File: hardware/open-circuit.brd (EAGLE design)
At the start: 90.2 x 40.6 mm, 72 parts, among them IC1 PIC16F1825SO14, IC2 74HC595D, IC3 MCP4728_QUAD_DAC, IC4 LM324D, IC6 LM27675M5_CHARGEPUMP

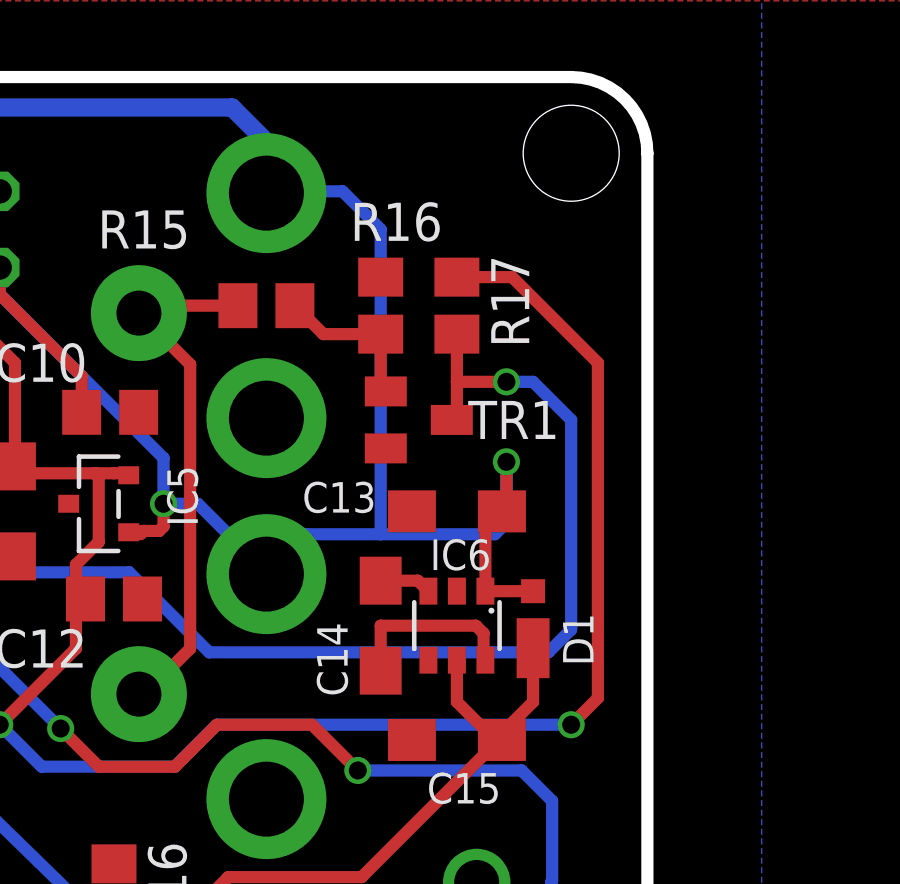
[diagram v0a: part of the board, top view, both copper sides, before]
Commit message: fix input transistor
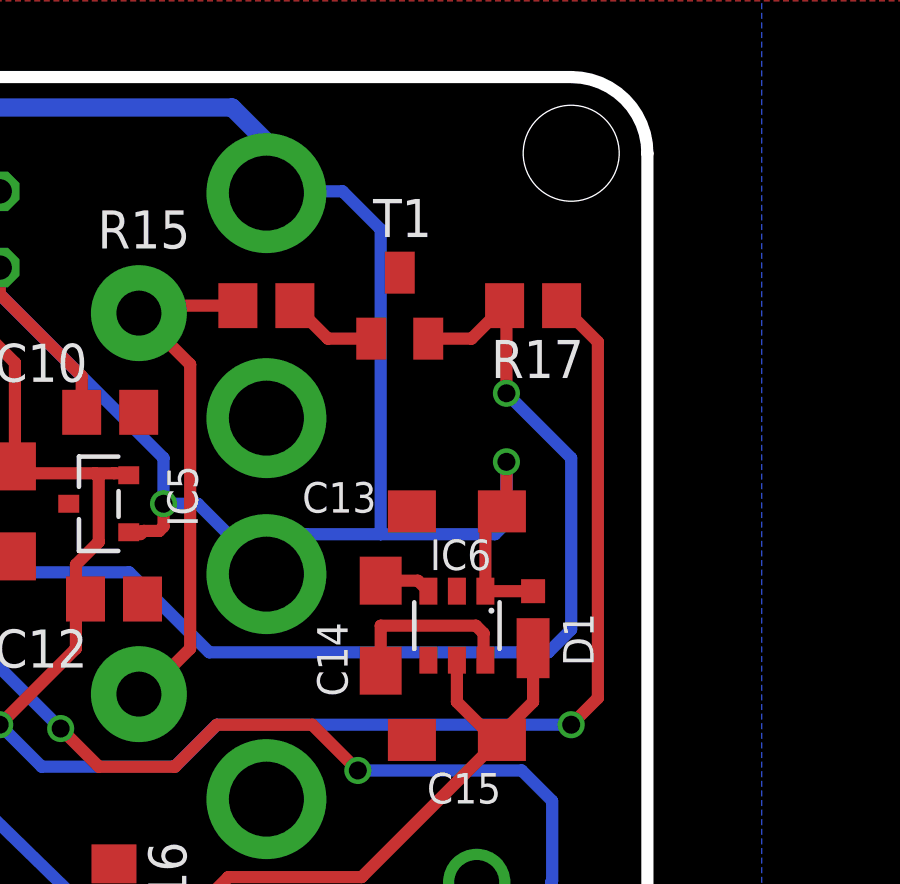
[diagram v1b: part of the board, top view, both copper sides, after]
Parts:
- removed R16: (no value), rcl:R0805
- removed TR1: (no value), transistor:SOT23-BEC
- added T1: (no value), transistor:SOT23-BEC
- moved R17 2.54 mm to (90.2, 77.5), turned to 180 degrees
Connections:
- removed net N$19: R15.1, R16.2, TR1.B
- new net N$14: R15.1, T1.B
- net GND: now also T1.C; no longer R16.1, TR1.E
- net MIDI_IN: now also T1.E; no longer TR1.C
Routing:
- net N$19: track 5.23 -> 0.00 mm
- net 3V3: track 102.9 -> 99.4 mm
- net N$14: track 0.00 -> 3.00 mm
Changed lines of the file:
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@@
 <attribute name="VALUE" x="76.2" y="72.644" size="0.4064" layer="27" rot="R90"/>
 </element>
-<element name="TR1" library="transistor" package="SOT23-BEC" value="" x="86.36" y="73.66" smashed="yes" rot="R270">
-<attribute name="NAME" x="88.011" y="73.025" size="1.27" layer="25"/>
-<attribute name="VALUE" x="83.185" y="75.565" size="1.27" layer="27" rot="R270"/>
-</element>
-<element name="R16" library="rcl" package="R0805" value="" x="85.09" y="77.47" smashed="yes" rot="R270">
-<attribute name="NAME" x="84.074" y="79.629" size="1.27" layer="25"/>
-<attribute name="VALUE" x="82.55" y="78.105" size="1.27" layer="27" rot="R270"/>
-</element>
-<element name="R17" library="rcl" package="R0805" value="" x="87.63" y="77.47" smashed="yes" rot="R270">
-<attribute name="NAME" x="90.043" y="76.073" size="1.27" layer="25" rot="R90"/>
-<attribute name="VALUE" x="85.09" y="78.105" size="1.27" layer="27" rot="R270"/>
+<element name="R17" library="rcl" package="R0805" value="" x="90.17" y="77.47" smashed="yes" rot="R180">
+<attribute name="NAME" x="88.773" y="75.057" size="1.27" layer="25"/>
+<attribute name="VALUE" x="90.805" y="80.01" size="1.27" layer="27" rot="R180"/>
 </element>
 <element name="C10" library="rcl" package="C0805" value="" x="76.073" y="73.914" smashed="yes" rot="R180">
@@
 <attribute name="NAME" x="88.646" y="56.896" size="1.27" layer="26" ratio="10" rot="MR270"/>
 <attribute name="VALUE" x="95.504" y="58.42" size="1.27" layer="28" ratio="10" rot="MR270"/>
+</element>
+<element name="T1" library="transistor" package="SOT23-BEC" value="" x="85.725" y="77.47" smashed="yes">
+<attribute name="NAME" x="84.836" y="79.756" size="1.27" layer="25"/>
+<attribute name="VALUE" x="83.82" y="74.295" size="1.27" layer="27"/>
 </element>
 </elements>
@@
 <contactref element="MIDI" pad="2"/>
 <contactref element="IC5" pad="3"/>
-<contactref element="TR1" pad="E"/>
 <contactref element="C12" pad="1"/>
 <contactref element="C13" pad="-"/>
 <contactref element="C10" pad="1"/>
-<contactref element="R16" pad="1"/>
 <contactref element="C11" pad="-"/>
 <contactref element="IC6" pad="2"/>
@@
 <via x="56.388" y="54.737" extent="1-16" drill="0.6"/>
 <contactref element="SW1" pad="2"/>
+<contactref element="T1" pad="C"/>
 </signal>
 <signal name="N$1">
@@
 </signal>
 <signal name="MIDI_IN">
-<contactref element="TR1" pad="C"/>
-<contactref element="R17" pad="2"/>
 <contactref element="IC1" pad="5"/>
-<wire x1="87.63" y1="73.83" x2="87.46" y2="73.66" width="0.4064" layer="1"/>
 <via x="60.452" y="67.691" extent="1-16" drill="0.6"/>
 <wire x1="58.36" y1="69.85" x2="59.944" y2="69.85" width="0.4064" layer="1"/>
 <wire x1="59.944" y1="69.85" x2="60.452" y2="69.342" width="0.4064" layer="1"/>
 <wire x1="60.452" y1="69.342" x2="60.452" y2="67.691" width="0.4064" layer="1"/>
-<wire x1="87.63" y1="73.83" x2="87.63" y2="74.93" width="0.4064" layer="1"/>
-<wire x1="87.63" y1="74.93" x2="89.281" y2="74.93" width="0.4064" layer="1"/>
-<via x="89.281" y="74.93" extent="1-16" drill="0.6"/>
-<wire x1="89.281" y1="74.93" x2="90.17" y2="74.93" width="0.4064" layer="16"/>
-<wire x1="90.17" y1="74.93" x2="91.44" y2="73.66" width="0.4064" layer="16"/>
-<wire x1="91.44" y1="73.66" x2="91.44" y2="66.675" width="0.4064" layer="16"/>
+<via x="89.281" y="74.549" extent="1-16" drill="0.6"/>
+<wire x1="89.281" y1="74.549" x2="91.44" y2="72.39" width="0.4064" layer="16"/>
+<wire x1="91.44" y1="72.39" x2="91.44" y2="66.675" width="0.4064" layer="16"/>
 <wire x1="91.44" y1="66.675" x2="90.678" y2="65.913" width="0.4064" layer="16"/>
 <wire x1="90.678" y1="65.913" x2="79.375" y2="65.913" width="0.4064" layer="16"/>
 <wire x1="79.375" y1="65.913" x2="76.708" y2="68.58" width="0.4064" layer="16"/>
-<wire x1="87.63" y1="76.52" x2="87.63" y2="74.93" width="0.4064" layer="1"/>
 <wire x1="60.452" y1="67.691" x2="66.421" y2="67.691" width="0.4064" layer="16"/>
 <wire x1="66.421" y1="67.691" x2="67.31" y2="68.58" width="0.4064" layer="16"/>
 <wire x1="67.31" y1="68.58" x2="76.708" y2="68.58" width="0.4064" layer="16"/>
+<contactref element="T1" pad="E"/>
+<contactref element="R17" pad="2"/>
+<wire x1="86.675" y1="76.37" x2="88.12" y2="76.37" width="0.4064" layer="1"/>
+<wire x1="88.12" y1="76.37" x2="89.22" y2="77.47" width="0.4064" layer="1"/>
+<wire x1="89.281" y1="74.549" x2="89.281" y2="77.409" width="0.4064" layer="1"/>
+<wire x1="89.281" y1="77.409" x2="89.22" y2="77.47" width="0.4064" layer="1"/>
 </signal>
 <signal name="3V3">
@@
 <wire x1="65.532" y1="75.311" x2="65.532" y2="76.962" width="0.4064" layer="16"/>
 <via x="65.532" y="76.962" extent="1-16" drill="0.6"/>
-<wire x1="87.63" y1="78.42" x2="89.474" y2="78.42" width="0.4064" layer="1"/>
-<wire x1="89.474" y1="78.42" x2="92.329" y2="75.565" width="0.4064" layer="1"/>
-<wire x1="92.329" y1="75.565" x2="92.329" y2="64.389" width="0.4064" layer="1"/>
+<wire x1="92.329" y1="76.261" x2="92.329" y2="64.389" width="0.4064" layer="1"/>
 <wire x1="92.329" y1="64.389" x2="91.44" y2="63.5" width="0.4064" layer="1"/>
 <via x="91.44" y="63.5" extent="1-16" drill="0.6"/>
@@
 <wire x1="75.692" y1="69.596" x2="75.692" y2="71.755" width="0.4064" layer="1"/>
 <wire x1="75.692" y1="71.755" x2="75.565" y2="71.882" width="0.4064" layer="1"/>
-</signal>
-<signal name="N$19">
-<contactref element="R16" pad="2"/>
-<contactref element="R15" pad="1"/>
-<contactref element="TR1" pad="B"/>
-<wire x1="85.09" y1="76.52" x2="83.18" y2="76.52" width="0.4064" layer="1"/>
-<wire x1="83.18" y1="76.52" x2="82.23" y2="77.47" width="0.4064" layer="1"/>
-<wire x1="85.09" y1="76.52" x2="85.09" y2="74.78" width="0.4064" layer="1"/>
-<wire x1="85.09" y1="74.78" x2="85.26" y2="74.61" width="0.4064" layer="1"/>
+<wire x1="92.329" y1="76.261" x2="91.12" y2="77.47" width="0.4064" layer="1"/>
 </signal>
 <signal name="N$20">
 <contactref element="MIDI" pad="3"/>
-<contactref element="R15" pad="2"/>
 <contactref element="THRU" pad="3"/>
-<wire x1="80.33" y1="77.47" x2="77.28" y2="77.47" width="0.4064" layer="1"/>
-<wire x1="77.28" y1="77.47" x2="77.03" y2="77.22" width="0.4064" layer="1"/>
 <wire x1="77.03" y1="64.52" x2="77.22" y2="64.52" width="0.4064" layer="1"/>
 <wire x1="77.22" y1="64.52" x2="78.74" y2="66.04" width="0.4064" layer="1"/>
 <wire x1="78.74" y1="66.04" x2="78.74" y2="75.51" width="0.4064" layer="1"/>
 <wire x1="78.74" y1="75.51" x2="77.03" y2="77.22" width="0.4064" layer="1"/>
+<contactref element="R15" pad="2"/>
+<wire x1="80.33" y1="77.47" x2="77.28" y2="77.47" width="0.4064" layer="1"/>
+<wire x1="77.28" y1="77.47" x2="77.03" y2="77.22" width="0.4064" layer="1"/>
 </signal>
 <signal name="N$23">
@@
 <wire x1="26.99" y1="64.77" x2="26.99" y2="64.201" width="0.4064" layer="1"/>
 </signal>
+<signal name="N$14">
+<contactref element="R15" pad="1"/>
+<contactref element="T1" pad="B"/>
+<wire x1="84.775" y1="76.37" x2="83.33" y2="76.37" width="0.4064" layer="1"/>
+<wire x1="83.33" y1="76.37" x2="82.23" y2="77.47" width="0.4064" layer="1"/>
+</signal>
 </signals>

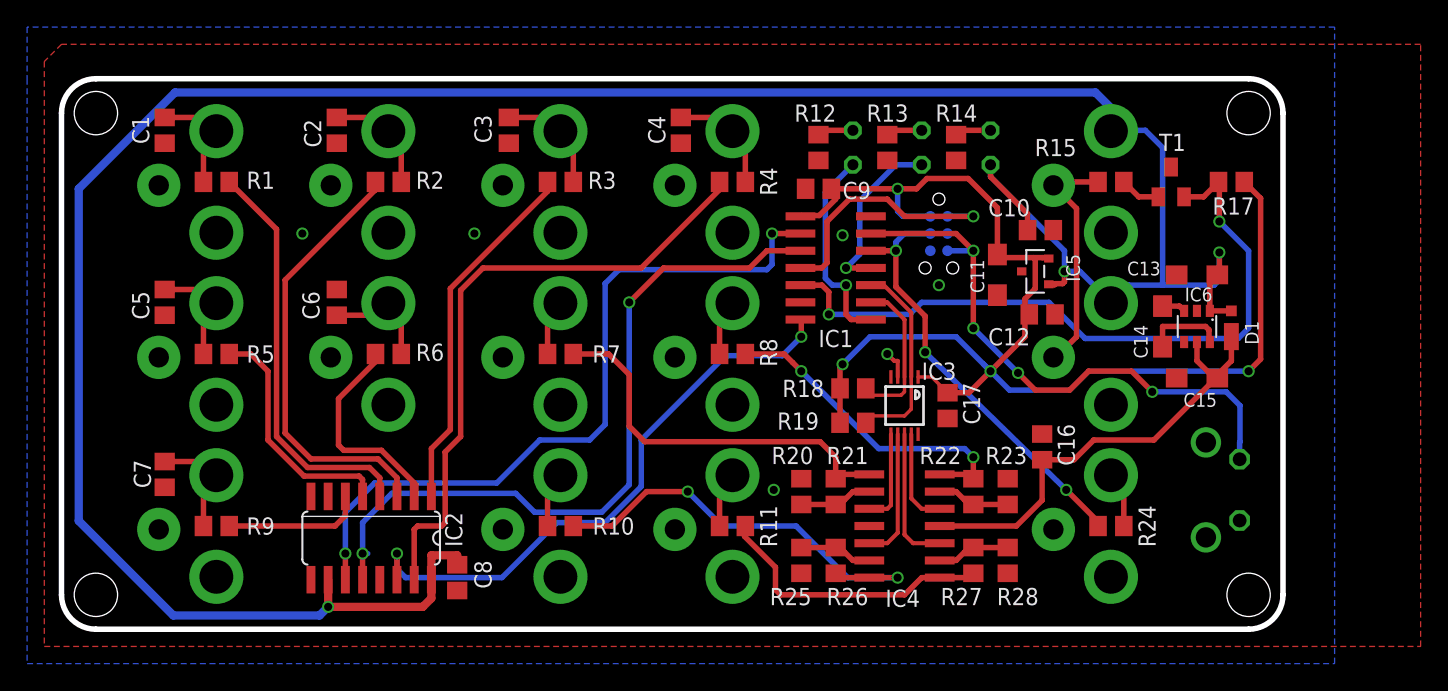
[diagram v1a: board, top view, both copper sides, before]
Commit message: add 5V voltage reg
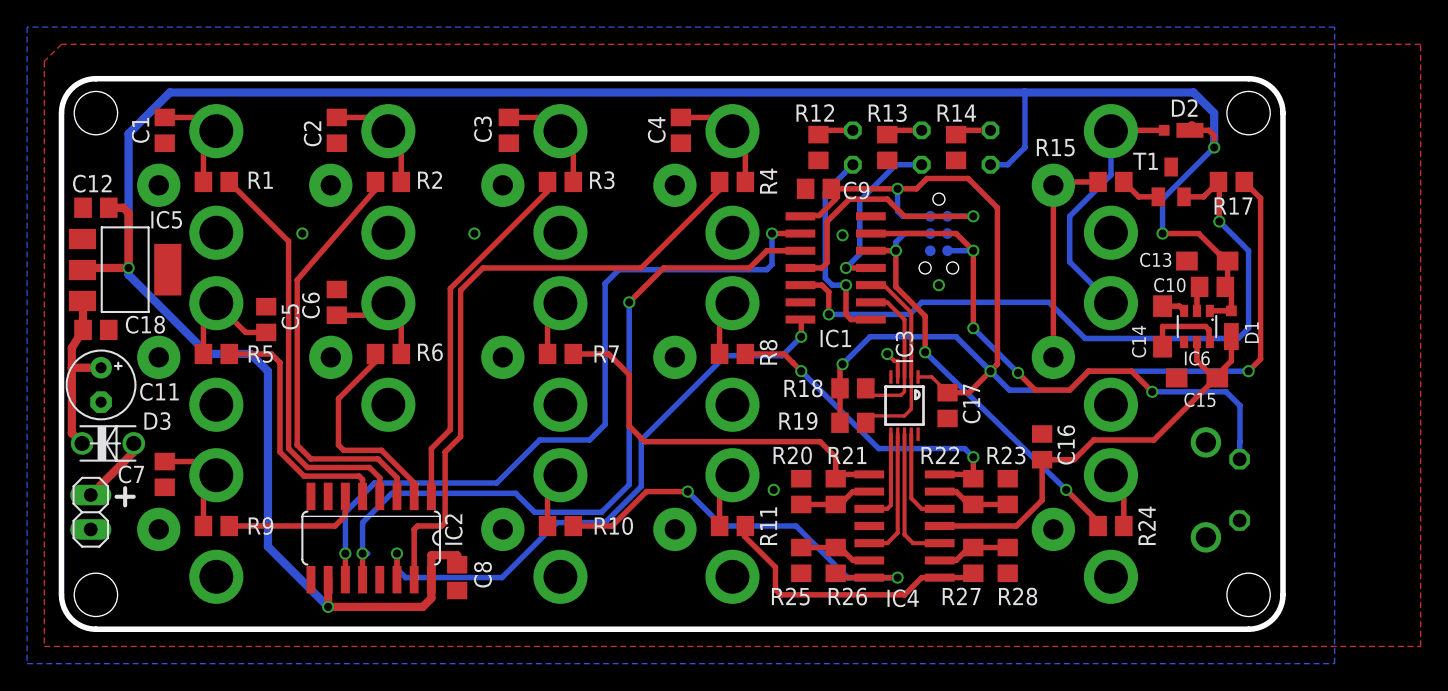
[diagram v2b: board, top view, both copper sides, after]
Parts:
- added C18: (no value), rcl:C0805
- added D2: PD3S160, diode:POWERDI323
- added D3: 1N4004, jasons_stuff:DO-VERT
- added JP1: (no value), pinhead:1X02
- C11: device rcl:SMC_A -> resistor:E2,5-5
- IC5: value (none) -> REG1117; device microbuilder:SOT23-R -> burr-brown:SOT223
- moved C12 70.3 mm to (6.35, 75.6), turned to 0 degrees
- moved IC5 67.2 mm to (8.51, 71.0), turned to 270 degrees
- moved C11 66.7 mm to (6.73, 62.5)
- moved C10 13.4 mm to (88.8, 69.7), turned to 0 degrees
- moved C5 7.60 mm to (18.9, 67.3), turned to 90 degrees
- moved C13 1.27 mm to (88.4, 71.6)
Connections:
- removed net 3V3: C11.+, C12.2, C17.2, C9.2, IC1.1, IC3.1, IC5.2, ISCP.2, R17.1, R18.1, R19.1
- removed net VIN: C10.2, C13.+, C8.1, D1.A, IC2.10, IC2.16, IC5.1, IC6.1, MIDI.4, PWR.A, THRU.4
- new net N$19: C11.+, C18.2, D3.C, IC5.3
- new net N$39: D2.A, MIDI.4, THRU.4
- new net N$40: D3.A, JP1.2
- new net VDD: C10.2, C12.2, C13.+, C17.2, C8.1, C9.2, D1.A, D2.C, IC1.1, IC2.10, IC2.16, IC3.1, IC5.2, IC6.1, ISCP.2, PWR.A, R17.1, R18.1, R19.1
- net GND: now also C18.1, IC5.1, JP1.1; no longer IC5.3
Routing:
- net VDD: track 0.00 -> 275.6 mm, vias 0 -> 8
- net VIN: track 199.1 -> 0.00 mm, vias 3 -> 0
- net 3V3: track 99.4 -> 0.00 mm, vias 4 -> 0
- net N$39: track 0.00 -> 19.2 mm
- net N$19: track 0.00 -> 13.2 mm
- net N$40: track 0.00 -> 5.13 mm
- net GND: track 2.16 -> 4.02 mm
- net N$20: track 17.6 -> 16.5 mm
- net N$16: track 32.3 -> 31.3 mm
- net N$17: track 17.9 -> 18.8 mm
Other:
- board text added: "midi to cv"
- board text added: "pcb rev 1"
- board text removed: "open circuit midi-cv"
- board text removed: "revision 1"

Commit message: change schottky footprint
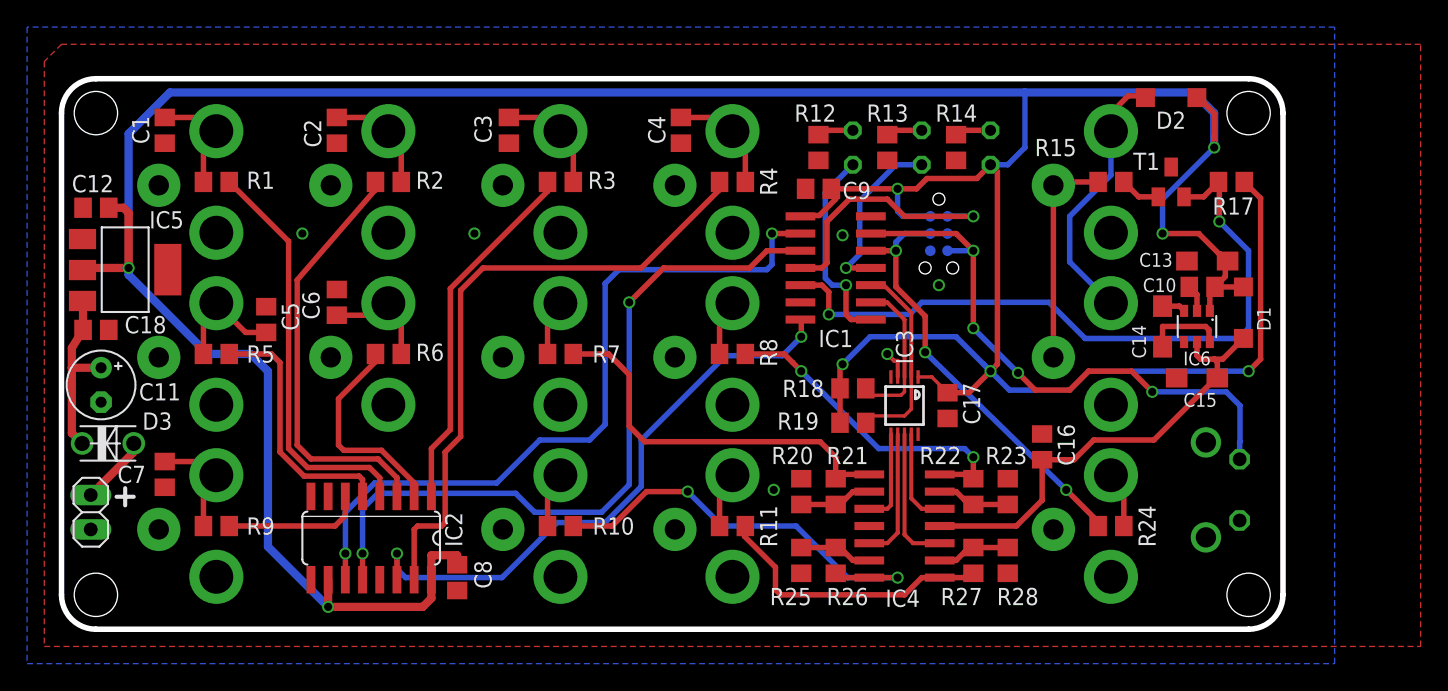
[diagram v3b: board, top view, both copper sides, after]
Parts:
- D1, D2: value PD3S160 -> MBR0520LT; device diode:POWERDI323 -> diode:SOD123
- moved D2 2.50 mm to (85.7, 83.7)
- moved D1 1.35 mm to (91.1, 67.8)
- moved C10 0.76 mm to (88.0, 69.7)
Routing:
- net VDD: track 275.6 -> 280.7 mm
- net N$39: track 19.2 -> 19.8 mm

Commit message: initial test of pcb
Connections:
- net CALIBRATE: now also ISCP.4; no longer ISCP.5
- net CAL_VIN: now also ISCP.5; no longer ISCP.4
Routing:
- net CALIBRATE: track 42.9 -> 41.0 mm
- net CAL_VIN: track 31.9 -> 30.0 mm
